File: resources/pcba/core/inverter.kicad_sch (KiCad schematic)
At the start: 29 parts, among them J10 INV LOAD, J11 RS485, J12 FAN, J9 INV BTN, Q1 PMOS IPD042P03L3, U10 L7805, U5 EL357N, U6 ADuM1201BR, U7 74LVC1G04, U8 MAX485E, U9 ADuM1200BR

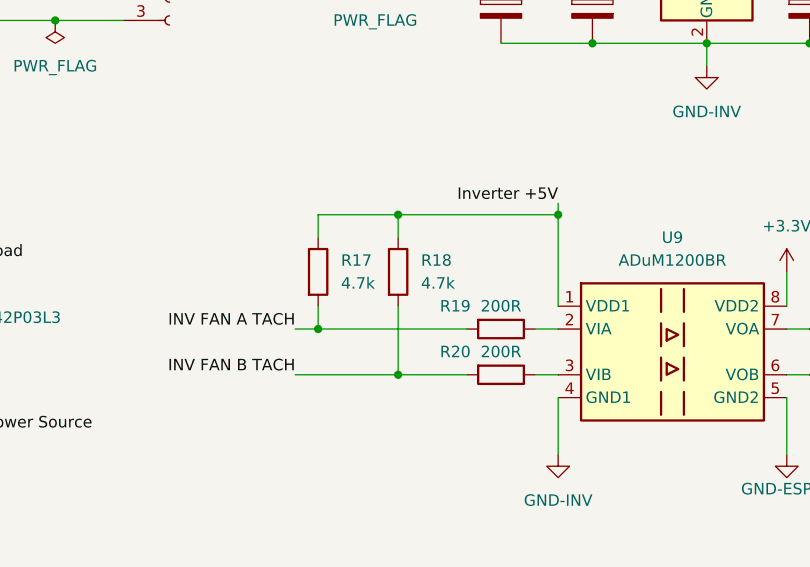
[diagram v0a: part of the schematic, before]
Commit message: update ble protocol
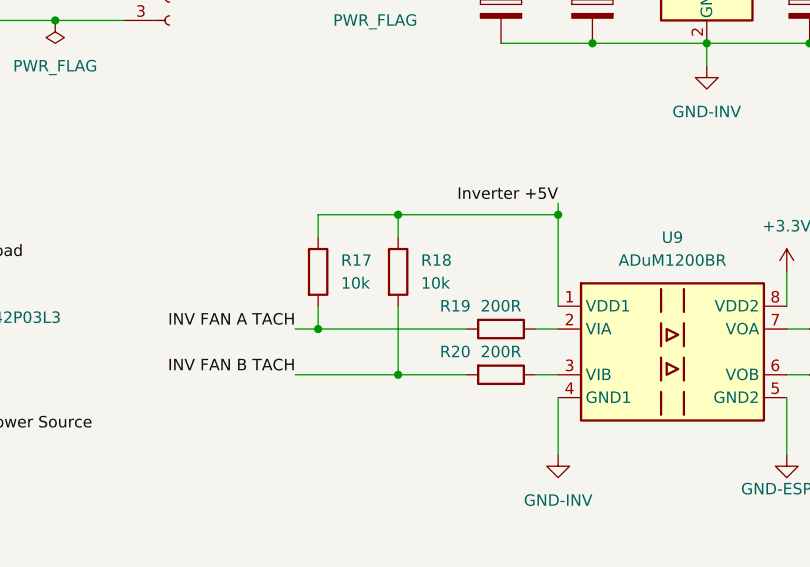
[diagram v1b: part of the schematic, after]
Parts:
- R17, R18: value 4.7k -> 10k
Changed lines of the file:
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@@
 			)
 		)
-		(property "Value" "4.7k"
+		(property "Value" "10k"
 			(at 144.78 64.7699 0)
 			(effects
@@
 			)
 		)
-		(property "Value" "4.7k"
+		(property "Value" "10k"
 			(at 135.89 64.7699 0)
 			(effects
